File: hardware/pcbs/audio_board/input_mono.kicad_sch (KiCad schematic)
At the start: 10 parts, among them J9 AudioJack3

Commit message: prepare for clock fanout
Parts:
- renumbered C57 to C60, C58 to C61, C59 to C62, R55 to R77, R56 to R78, R57 to R79, R58 to R80

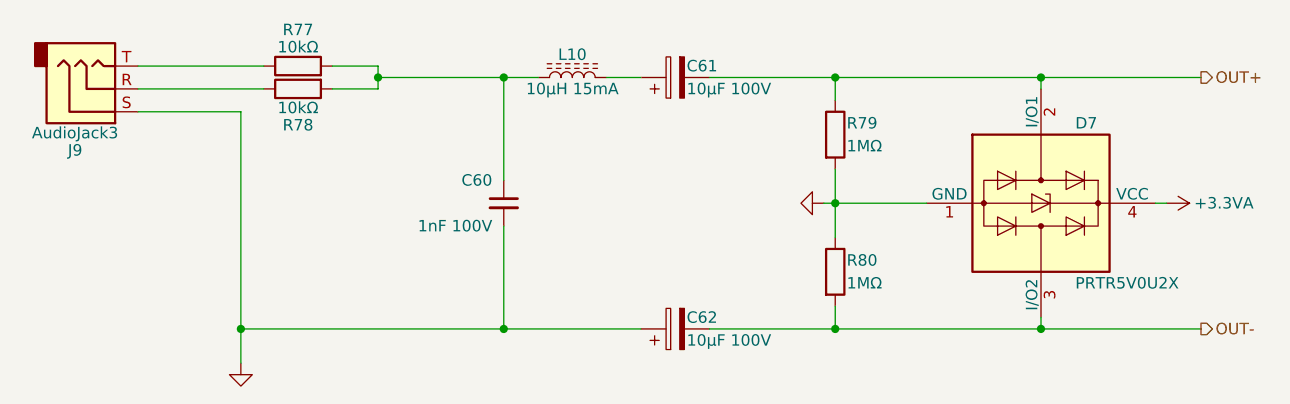
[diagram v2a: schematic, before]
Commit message: audioboard: route clock fanout
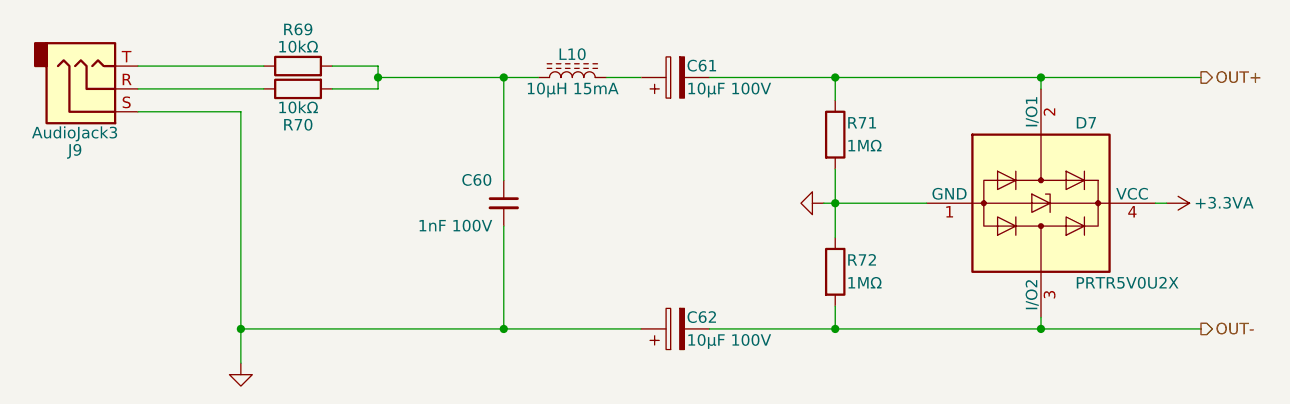
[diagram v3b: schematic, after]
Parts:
- renumbered R77 to R69, R78 to R70, R79 to R71, R80 to R72
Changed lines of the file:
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@@
 		(in_pos_files yes)
 		(dnp no)
-		(property "Reference" "R80"
+		(property "Reference" "R72"
 			(at 166.37 115.57 0)
 			(show_name no)
@@
 			(project "audio_board"
 				(path "/54443f96-c7c5-4432-b890-45b14a1547a1/c7838b89-33be-4400-baf7-0a033ee6e87f"
-					(reference "R80")
+					(reference "R72")
 					(unit 1)
 				)
@@
 		(in_pos_files yes)
 		(dnp no)
-		(property "Reference" "R79"
+		(property "Reference" "R71"
 			(at 166.37 100.33 0)
 			(show_name no)
@@
 			(project "audio_board"
 				(path "/54443f96-c7c5-4432-b890-45b14a1547a1/c7838b89-33be-4400-baf7-0a033ee6e87f"
-					(reference "R79")
+					(reference "R71")
 					(unit 1)
 				)
@@
 		(dnp no)
 		(fields_autoplaced yes)
-		(property "Reference" "R77"
+		(property "Reference" "R69"
 			(at 105.41 89.9541 90)
 			(show_name no)
@@
 			(project "audio_board"
 				(path "/54443f96-c7c5-4432-b890-45b14a1547a1/c7838b89-33be-4400-baf7-0a033ee6e87f"
-					(reference "R77")
+					(reference "R69")
 					(unit 1)
 				)
@@
 		(in_pos_files yes)
 		(dnp no)
-		(property "Reference" "R78"
+		(property "Reference" "R70"
 			(at 105.41 100.5459 90)
 			(show_name no)
@@
 			(project "audio_board"
 				(path "/54443f96-c7c5-4432-b890-45b14a1547a1/c7838b89-33be-4400-baf7-0a033ee6e87f"
-					(reference "R78")
+					(reference "R70")
 					(unit 1)
 				)

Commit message: audioboard: finalise routing
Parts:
- renumbered R69 to R71, R70 to R72, R71 to R73, R72 to R74
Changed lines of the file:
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@@
 		(in_pos_files yes)
 		(dnp no)
-		(property "Reference" "R72"
+		(property "Reference" "R74"
 			(at 166.37 115.57 0)
 			(show_name no)
@@
 			(project "audio_board"
 				(path "/54443f96-c7c5-4432-b890-45b14a1547a1/c7838b89-33be-4400-baf7-0a033ee6e87f"
-					(reference "R72")
+					(reference "R74")
 					(unit 1)
 				)
@@
 		(in_pos_files yes)
 		(dnp no)
-		(property "Reference" "R71"
+		(property "Reference" "R73"
 			(at 166.37 100.33 0)
 			(show_name no)
@@
 			(project "audio_board"
 				(path "/54443f96-c7c5-4432-b890-45b14a1547a1/c7838b89-33be-4400-baf7-0a033ee6e87f"
-					(reference "R71")
+					(reference "R73")
 					(unit 1)
 				)
@@
 		(dnp no)
 		(fields_autoplaced yes)
-		(property "Reference" "#PWR0126"
+		(property "Reference" "#PWR0127"
 			(at 157.48 109.22 0)
 			(hide yes)
@@
 			(project "audio_board"
 				(path "/54443f96-c7c5-4432-b890-45b14a1547a1/c7838b89-33be-4400-baf7-0a033ee6e87f"
-					(reference "#PWR0126")
+					(reference "#PWR0127")
 					(unit 1)
 				)
@@
 		(dnp no)
 		(fields_autoplaced yes)
-		(property "Reference" "#PWR0125"
+		(property "Reference" "#PWR0126"
 			(at 99.06 133.35 0)
 			(hide yes)
@@
 			(project "audio_board"
 				(path "/54443f96-c7c5-4432-b890-45b14a1547a1/c7838b89-33be-4400-baf7-0a033ee6e87f"
-					(reference "#PWR0125")
+					(reference "#PWR0126")
 					(unit 1)
 				)
@@
 		(dnp no)
 		(fields_autoplaced yes)
-		(property "Reference" "R69"
+		(property "Reference" "R71"
 			(at 105.41 89.9541 90)
 			(show_name no)
@@
 			(project "audio_board"
 				(path "/54443f96-c7c5-4432-b890-45b14a1547a1/c7838b89-33be-4400-baf7-0a033ee6e87f"
-					(reference "R69")
+					(reference "R71")
 					(unit 1)
 				)
@@
 		(in_pos_files yes)
 		(dnp no)
-		(property "Reference" "#PWR0127"
+		(property "Reference" "#PWR0128"
 			(at 198.12 109.22 0)
 			(hide yes)
@@
 			(project "audio_board"
 				(path "/54443f96-c7c5-4432-b890-45b14a1547a1/c7838b89-33be-4400-baf7-0a033ee6e87f"
-					(reference "#PWR0127")
+					(reference "#PWR0128")
 					(unit 1)
 				)
@@
 		(in_pos_files yes)
 		(dnp no)
-		(property "Reference" "R70"
+		(property "Reference" "R72"
 			(at 105.41 100.5459 90)
 			(show_name no)
@@
 			(project "audio_board"
 				(path "/54443f96-c7c5-4432-b890-45b14a1547a1/c7838b89-33be-4400-baf7-0a033ee6e87f"
-					(reference "R70")
+					(reference "R72")
 					(unit 1)
 				)

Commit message: minor changes to audioboard
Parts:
- renumbered R71 to R69, R72 to R70, R73 to R71, R74 to R72
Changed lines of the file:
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@@
 		(in_pos_files yes)
 		(dnp no)
-		(property "Reference" "R74"
+		(property "Reference" "R72"
 			(at 166.37 115.57 0)
 			(show_name no)
@@
 			(project "audio_board"
 				(path "/54443f96-c7c5-4432-b890-45b14a1547a1/c7838b89-33be-4400-baf7-0a033ee6e87f"
-					(reference "R74")
+					(reference "R72")
 					(unit 1)
 				)
@@
 		(in_pos_files yes)
 		(dnp no)
-		(property "Reference" "R73"
+		(property "Reference" "R71"
 			(at 166.37 100.33 0)
 			(show_name no)
@@
 			(project "audio_board"
 				(path "/54443f96-c7c5-4432-b890-45b14a1547a1/c7838b89-33be-4400-baf7-0a033ee6e87f"
-					(reference "R73")
+					(reference "R71")
 					(unit 1)
 				)
@@
 		(dnp no)
 		(fields_autoplaced yes)
-		(property "Reference" "R71"
+		(property "Reference" "R69"
 			(at 105.41 89.9541 90)
 			(show_name no)
@@
 			(project "audio_board"
 				(path "/54443f96-c7c5-4432-b890-45b14a1547a1/c7838b89-33be-4400-baf7-0a033ee6e87f"
-					(reference "R71")
+					(reference "R69")
 					(unit 1)
 				)
@@
 		(in_pos_files yes)
 		(dnp no)
-		(property "Reference" "R72"
+		(property "Reference" "R70"
 			(at 105.41 100.5459 90)
 			(show_name no)
@@
 			(project "audio_board"
 				(path "/54443f96-c7c5-4432-b890-45b14a1547a1/c7838b89-33be-4400-baf7-0a033ee6e87f"
-					(reference "R72")
+					(reference "R70")
 					(unit 1)
 				)
